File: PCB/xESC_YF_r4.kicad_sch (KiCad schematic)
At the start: 30 parts, among them J1 Conn_01x09_Male, J10 OM-MB W => MC BRK, J11 Conn_01x04_Pin, J3 Conn_01x05_Male, J4 Conn_01x05_Male, J6 OM-MB U => MC SA, J7 Conn_01x06_Male, J8 Conn_01x06_Pin, J9 OM-MB V => MC +24V, U1 STM32C011F6Px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

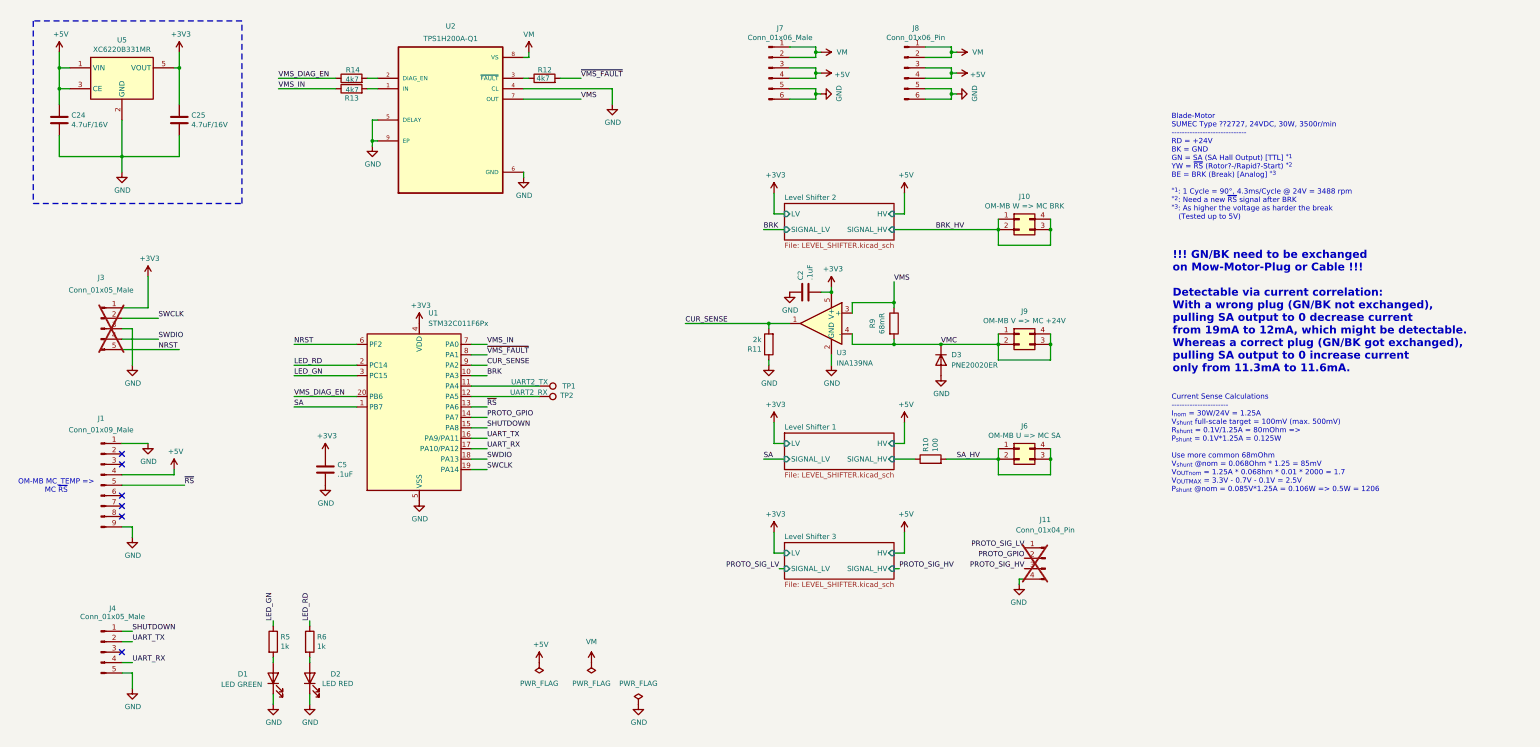
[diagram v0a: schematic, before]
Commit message: 2 stage current sense with 20/40 gain
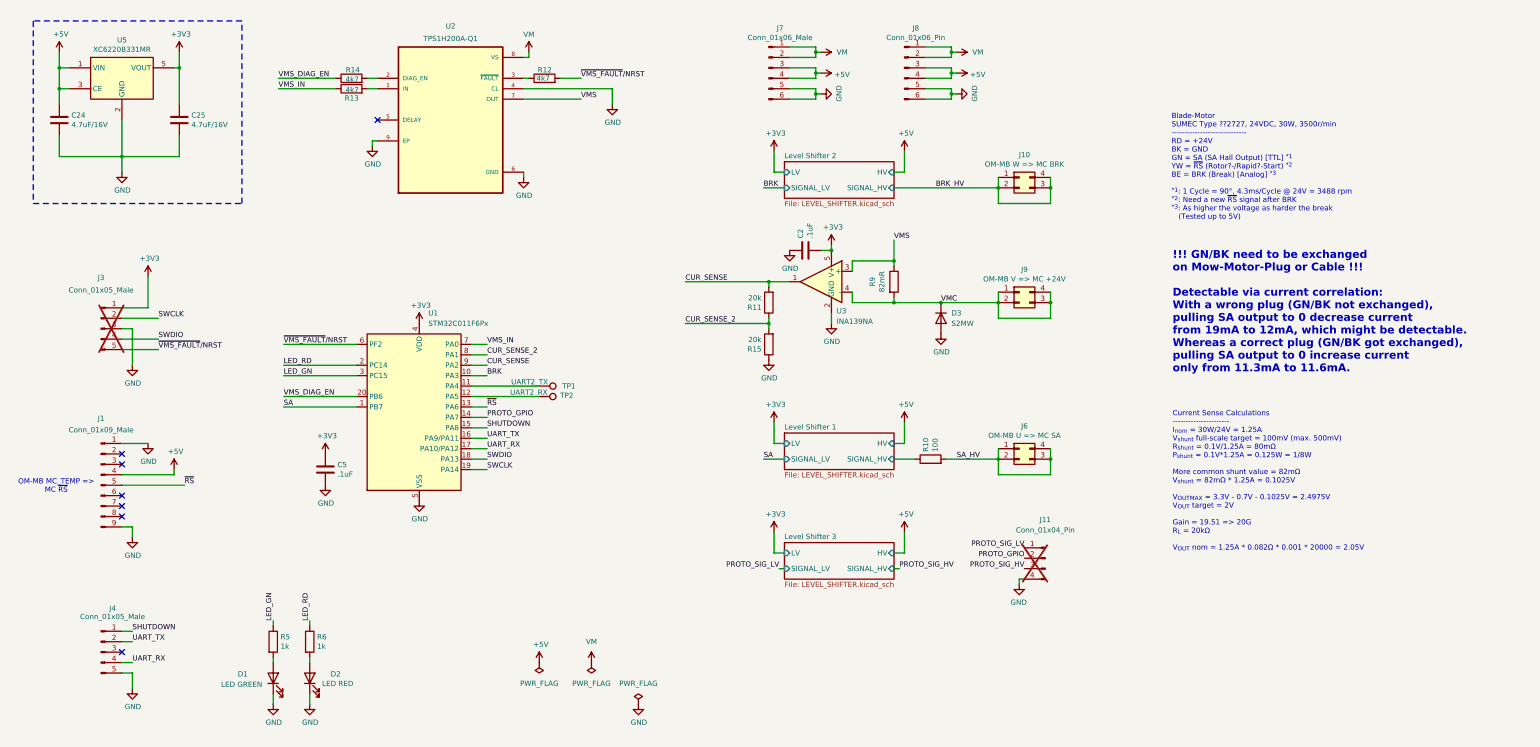
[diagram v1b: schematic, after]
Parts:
- added R15: 20k, Resistor_SMD:R_0402_1005Metric, symbol Device:R
- D3: value PNE20020ER -> S2MW; footprint Diode_SMD:Nexperia_CFP3_SOD-123W -> Diode_SMD:D_SOD-123F; JLCPCB (none) -> C2900725; Part Number (none) -> S2MW
- R11: value 2k -> 20k; footprint Resistor_SMD:R_0603_1608Metric -> Resistor_SMD:R_0402_1005Metric; JLCPCB (none) -> C2579762; Part Number (none) -> RK73G1ETTP2002D; Stock_PN (none) -> R-0402-20000-0.1W-0.5%
- R9: value 68mR -> 82mR; footprint Resistor_SMD:R_1206_3216Metric_Pad1.30x1.75mm_HandSolder -> Resistor_SMD:R_0805_2012Metric_Pad1.20x1.40mm_HandSolder; JLCPCB C2442650 -> C2442701; Part Number KDV12FR068ET -> KDV08FR082ET; Stock_PN R-1206-.080-0.5W-1% -> R-0805-.082-0.25W-1%
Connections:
- net GND: now also R15.1; no longer R11.1, U2.5 (DELAY)
- net NRST renamed ~{VMS_FAULT}/NRST
- net ~{VMS_FAULT}/NRST: now also R12.2
- net ~{VMS_FAULT} renamed CUR_SENSE_2
- net CUR_SENSE_2: now also R11.1, R15.2; no longer R12.2
- no-connect marks 6 -> 7
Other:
- note added: "Current Sense Calculations ---------------------- I_{nom} = 30W/24V = 1.25A V_{shunt} full-scale target = 100mV (max. 500mV) R_{shunt} = 0.1V/1.25A = 80mΩ P_{shunt} = 0.1V*1.25A = 0.125W = 1/8W More common shunt value = 82mΩ V_{shunt} = 82mΩ * 1.25A = 0.1025V V_{OUTMAX} = 3.3V - 0.7V - 0.1025V = 2.4975V V_{OUT} target = 2V Gain = 19.51 => 20G R_{L} = 20kΩ V_{OUT} nom = 1.25A * 0.082Ω * 0.001 * 20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"
- note removed: "Current Sense Calculations ---------------------- I_{nom} = 30W/24V = 1.25A V_{shunt} full-scale target = 100mV (max. 500mV) R_{shunt} = 0.1V/1.25A = 80mOhm => P_{shunt} = 0.1V*1.25A = 0.125W Use more common 68mOhm V_{shunt} @nom = 0.068Ohm * 1.25 = 85mV V_{OUTnom} = 1.25A * 0.068hm * 0.01 * 2000 = 1.7 V_{OUTMAX} = 3.3V - 0.7V - 0.1V = 2.5V P_{shunt} @nom = 0.085V*1.25A = 0.106W => 0.5W = 1206"
- moved on the sheet: C2, D3, J10, J9, R11, R9, U3

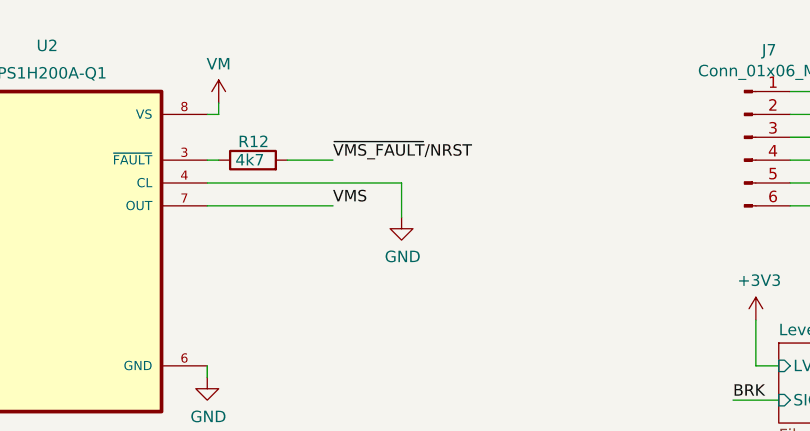
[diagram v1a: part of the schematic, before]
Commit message: Open-load detection
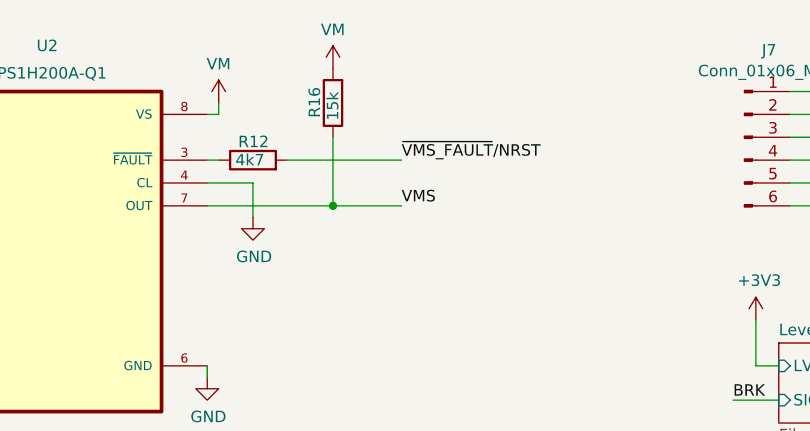
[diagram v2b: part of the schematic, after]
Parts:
- added R16: 15k, Resistor_SMD:R_0603_1608Metric, symbol Device:R
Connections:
- net VM: now also R16.2
- net VMS: now also R16.1
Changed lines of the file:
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@@
 	)
 	(junction
+		(at 153.67 38.1)
+		(diameter 0)
+		(color 0 0 0 0)
+	)
+	(junction
 		(at 199.39 82.55)
 		(diameter 0)
@@
 	(wire
 		(pts
-			(xy 153.67 38.1) (xy 139.7 38.1)
+			(xy 161.29 38.1) (xy 153.67 38.1)
 		)
 		(stroke
@@
 	(wire
 		(pts
+			(xy 153.67 30.48) (xy 153.67 38.1)
+		)
+		(stroke
+			(width 0)
+			(type default)
+		)
+	)
+	(wire
+		(pts
 			(xy 199.39 91.44) (xy 199.39 92.71)
 		)
@@
 		)
 	)
+	(wire
+		(pts
+			(xy 153.67 38.1) (xy 139.7 38.1)
+		)
+		(stroke
+			(width 0)
+			(type default)
+		)
+	)
 	(polyline
 		(pts
@@
 	(wire
 		(pts
-			(xy 153.67 33.02) (xy 148.59 33.02)
+			(xy 161.29 33.02) (xy 148.59 33.02)
 		)
 		(stroke
@@
 	(wire
 		(pts
-			(xy 139.7 35.56) (xy 161.29 35.56)
+			(xy 139.7 35.56) (xy 144.78 35.56)
 		)
 		(stroke
@@
 	(wire
 		(pts
-			(xy 161.29 35.56) (xy 161.29 39.37)
+			(xy 144.78 35.56) (xy 144.78 39.37)
 		)
 		(stroke
@@
 	)
 	(label "~{VMS_FAULT}{slash}NRST"
-		(at 153.67 33.02 0)
+		(at 161.29 33.02 0)
 		(fields_autoplaced yes)
 		(effects
@@
 	)
 	(label "VMS"
-		(at 153.67 38.1 0)
+		(at 161.29 38.1 0)
 		(fields_autoplaced yes)
 		(effects
@@
 	)
 	(symbol
+		(lib_id "Device:R")
+		(at 153.67 26.67 180)
+		(unit 1)
+		(exclude_from_sim no)
+		(in_bom yes)
+		(on_board yes)
+		(dnp no)
+		(property "Reference" "R16"
+			(at 151.638 24.892 90)
+			(effects
+				(font
+					(size 1.27 1.27)
+				)
+				(justify left)
+			)
+		)
+		(property "Value" "15k"
+			(at 153.67 25.4 90)
+			(effects
+				(font
+					(size 1.27 1.27)
+				)
+				(justify left)
+			)
+		)
+		(property "Footprint" "Resistor_SMD:R_0603_1608Metric"
+			(at 155.448 26.67 90)
+			(effects
+				(font
+					(size 1.27 1.27)
+				)
+				(hide yes)
+			)
+		)
+		(property "Datasheet" "~"
+			(at 153.67 26.67 0)
+			(effects
+				(font
+					(size 1.27 1.27)
+				)
+				(hide yes)
+			)
+		)
+		(property "Description" "Resistor"
+			(at 153.67 26.67 0)
+			(effects
+				(font
+					(size 1.27 1.27)
+				)
+				(hide yes)
+			)
+		)
+		(property "Part Number" ""
+			(at 153.67 26.67 0)
+			(effects
+				(font
+					(size 1.27 1.27)
+				)
+				(hide yes)
+			)
+		)
+		(property "Stock_PN" "R-603-15000-.1W-1%"
+			(at 153.67 26.67 0)
+			(effects
+				(font
+					(size 1.27 1.27)
+				)
+				(hide yes)
+			)
+		)
+		(pin "1"
+		)
+		(pin "2"
+		)
+		(instances
+			(project "xESC_YF_r4"
+				(path "/f1d82565-2f45-4436-9c4d-3203604bc842"
+					(reference "R16")
+					(unit 1)
+				)
+			)
+		)
+	)
+	(symbol
 		(lib_id "power:+5V")
 		(at 232.41 50.8 0)
@@
 	)
 	(symbol
+		(lib_id "power:+BATT")
+		(at 153.67 22.86 0)
+		(unit 1)
+		(exclude_from_sim no)
+		(in_bom yes)
+		(on_board yes)
+		(dnp no)
+		(property "Reference" "#PWR040"
+			(at 153.67 26.67 0)
+			(effects
+				(font
+					(size 1.27 1.27)
+				)
+				(hide yes)
+			)
+		)
+		(property "Value" "VM"
+			(at 153.67 18.542 0)
+			(effects
+				(font
+					(size 1.27 1.27)
+				)
+			)
+		)
+		(property "Footprint" ""
+			(at 153.67 22.86 0)
+			(effects
+				(font
+					(size 1.27 1.27)
+				)
+				(hide yes)
+			)
+		)
+		(property "Datasheet" ""
+			(at 153.67 22.86 0)
+			(effects
+				(font
+					(size 1.27 1.27)
+				)
+				(hide yes)
+			)
+		)
+		(property "Description" "Power symbol creates a global label with name \"+BATT\""
+			(at 153.67 22.86 0)
+			(effects
+				(font
+					(size 1.27 1.27)
+				)
+				(hide yes)
+			)
+		)
+		(pin "1"
+		)
+		(instances
+			(project "xESC_YF_r4"
+				(path "/f1d82565-2f45-4436-9c4d-3203604bc842"
+					(reference "#PWR040")
+					(unit 1)
+				)
+			)
+		)
+	)
+	(symbol
 		(lib_id "Device:R")
 		(at 229.87 82.55 0)
@@
 	(symbol
 		(lib_id "power:GND")
-		(at 161.29 39.37 0)
+		(at 144.78 39.37 0)
 		(unit 1)
 		(exclude_from_sim no)
@@
 		(dnp no)
 		(property "Reference" "#PWR038"
-			(at 161.29 45.72 0)
+			(at 144.78 45.72 0)
 			(effects
 				(font
@@
 		)
 		(property "Value" "GND"
-			(at 161.417 43.7642 0)
+			(at 144.907 43.7642 0)
 			(effects
 				(font
@@
 		)
 		(property "Footprint" ""
-			(at 161.29 39.37 0)
+			(at 144.78 39.37 0)
 			(effects
 				(font
@@
 		)
 		(property "Datasheet" ""
-			(at 161.29 39.37 0)
+			(at 144.78 39.37 0)
 			(effects
 				(font
@@
 		)
 		(property "Description" "Power symbol creates a global label with name \"GND\" , ground"
-			(at 161.29 39.37 0)
+			(at 144.78 39.37 0)
 			(effects
 				(font

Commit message: Fix DRC issues
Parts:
- U2: footprint TPS1H200AQDGNRQ1:SOP65P490X110-9N-AHMOD -> TPS1H200AQDGNRQ1.snapeda:SOP65P490X110-9N; AVAILABILITY In Stock -> (none); Availability In Stock -> (none); CHECK_PRICES https://www.snapeda.com/parts/TPS1H200AQDGNRQ1/Texas+Instru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 -> (none); Check_prices https://www.snapeda.com/parts/TPS1H200AQDGNRQ1/Texas+Instru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 -> (none); DESCRIPTION 40-V, 200-mΩ, 1-ch automotive smart high-side switch with a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 -> (none); Description_1 40-V, 200-mΩ, 1-ch automotive smart high-side switch with a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 -> (none); MF Texas Instruments -> (none); MP TPS1H200AQDGNRQ1 -> (none); PACKAGE HVSSOP-8 Texas Instruments -> (none); PRICE None -> (none); PURCHASE-URL https://www.snapeda.com/api/url_track_click_mouser/?unipart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 -> (none); Price None -> (none); Purchase-URL https://www.snapeda.com/api/url_track_click_mouser/?unipart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 -> (none); SNAPEDA_LINK https://www.snapeda.com/parts/TPS1H200AQDGNRQ1/Texas+Instru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 -> (none); SnapEDA_Link https://www.snapeda.com/parts/TPS1H200AQDGNRQ1/Texas+Instru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 -> (none)
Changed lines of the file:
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@@
 			)
 		)
-		(property "Footprint" "TPS1H200AQDGNRQ1:SOP65P490X110-9N-AHMOD"
+		(property "Footprint" "TPS1H200AQDGNRQ1.snapeda:SOP65P490X110-9N"
 			(at 121.92 43.18 0)
 			(effects
@@
 			)
 		)
-		(property "Description" ""
+		(property "Description" "40-V, 200-mΩ, 1-ch automotive smart high-side switch with adjustable current limit"
 			(at 121.92 43.18 0)
 			(effects
@@
 			)
 		)
-		(property "SNAPEDA_LINK" "https://www.snapeda.com/parts/TPS1H200AQDGNRQ1/Texas+Instruments/view-part/?ref=snap"
-			(at 121.92 43.18 0)
-			(effects
-				(font
-					(size 1.27 1.27)
-				)
-				(justify bottom)
-				(hide yes)
-			)
-		)
-		(property "CHECK_PRICES" "https://www.snapeda.com/parts/TPS1H200AQDGNRQ1/Texas+Instruments/view-part/?ref=eda"
-			(at 121.92 43.18 0)
-			(effects
-				(font
-					(size 1.27 1.27)
-				)
-				(justify bottom)
-				(hide yes)
-			)
-		)
-		(property "PURCHASE-URL" "https://www.snapeda.com/api/url_track_click_mouser/?unipart_id=3210362&manufacturer=Texas Instruments&part_name=TPS1H200AQDGNRQ1&search_term=tps1h200aqdgnrq1"
-			(at 121.92 43.18 0)
-			(effects
-				(font
-					(size 1.27 1.27)
-				)
-				(justify bottom)
-				(hide yes)
-			)
-		)
-		(property "PACKAGE" "HVSSOP-8 Texas Instruments"
-			(at 121.92 43.18 0)
-			(effects
-				(font
-					(size 1.27 1.27)
-				)
-				(justify bottom)
-				(hide yes)
-			)
-		)
-		(property "PRICE" "None"
-			(at 121.92 43.18 0)
-			(effects
-				(font
-					(size 1.27 1.27)
-				)
-				(justify bottom)
-				(hide yes)
-			)
-		)
 		(property "Package" "HVSSOP-8 Texas Instruments"
 			(at 121.92 43.18 0)
 			(effects
-				(font
-					(size 1.27 1.27)
-				)
-				(justify bottom)
-				(hide yes)
-			)
-		)
-		(property "Check_prices" "https://www.snapeda.com/parts/TPS1H200AQDGNRQ1/Texas+Instruments/view-part/?ref=eda"
-			(at 121.92 43.18 0)
-			(effects
-				(font
-					(size 1.27 1.27)
-				)
-				(justify bottom)
-				(hide yes)
-			)
-		)
-		(property "SnapEDA_Link" "https://www.snapeda.com/parts/TPS1H200AQDGNRQ1/Texas+Instruments/view-part/?ref=snap"
-			(at 121.92 43.18 0)
-			(effects
-				(font
-					(size 1.27 1.27)
-				)
-				(justify bottom)
-				(hide yes)
-			)
-		)
-		(property "Price" "None"
-			(at 121.92 43.18 0)
-			(effects
-				(font
-					(size 1.27 1.27)
-				)
-				(justify bottom)
-				(hide yes)
-			)
-		)
-		(property "MF" "Texas Instruments"
-			(at 121.92 43.18 0)
-			(effects
-				(font
-					(size 1.27 1.27)
-				)
-				(justify bottom)
-				(hide yes)
-			)
-		)
-		(property "MP" "TPS1H200AQDGNRQ1"
-			(at 121.92 43.18 0)
-			(effects
-				(font
-					(size 1.27 1.27)
-				)
-				(justify bottom)
-				(hide yes)
-			)
-		)
-		(property "Purchase-URL" "https://www.snapeda.com/api/url_track_click_mouser/?unipart_id=3210362&manufacturer=Texas Instruments&part_name=TPS1H200AQDGNRQ1&search_term=tps1h200"
-			(at 121.92 43.18 0)
-			(effects
-				(font
-					(size 1.27 1.27)
-				)
-				(justify bottom)
-				(hide yes)
-			)
-		)
-		(property "Description_1" "\n40-V, 200-mΩ, 1-ch automotive smart high-side switch with adjustable current limit\n"
-			(at 121.92 43.18 0)
-			(effects
-				(font
-					(size 1.27 1.27)
-				)
-				(justify bottom)
-				(hide yes)
-			)
-		)
-		(property "Availability" "In Stock"
-			(at 121.92 43.18 0)
-			(effects
-				(font
-					(size 1.27 1.27)
-				)
-				(justify bottom)
-				(hide yes)
-			)
-		)
-		(property "AVAILABILITY" "In Stock"
-			(at 121.92 43.18 0)
-			(effects
-				(font
-					(size 1.27 1.27)
-				)
-				(justify bottom)
-				(hide yes)
-			)
-		)
-		(property "DESCRIPTION" "40-V, 200-mΩ, 1-ch automotive smart high-side switch with adjustable current limit"
-			(at 121.92 43.18 0)
-			(effects
